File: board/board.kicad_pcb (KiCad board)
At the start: 2 copper layers, 21 x 13 mm, 1 part

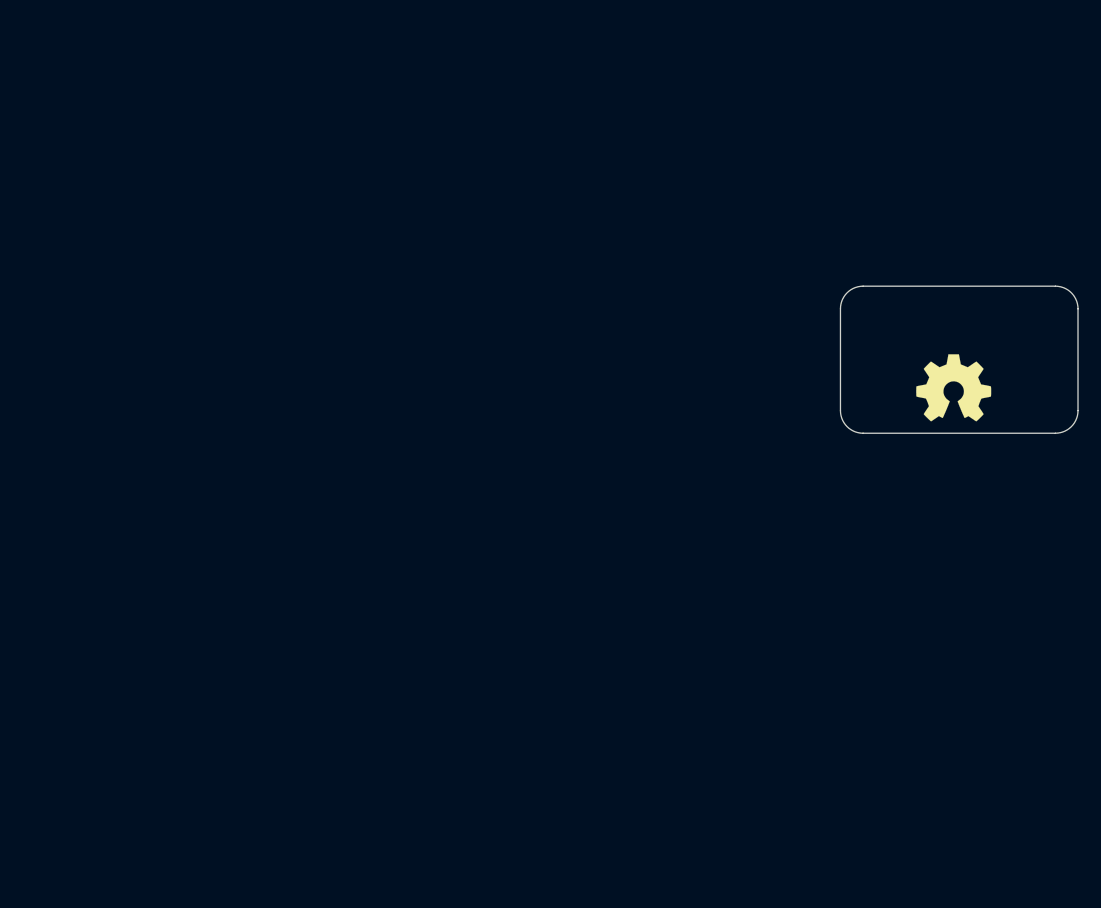
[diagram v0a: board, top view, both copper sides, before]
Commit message: added schematic and footprint from legacy project
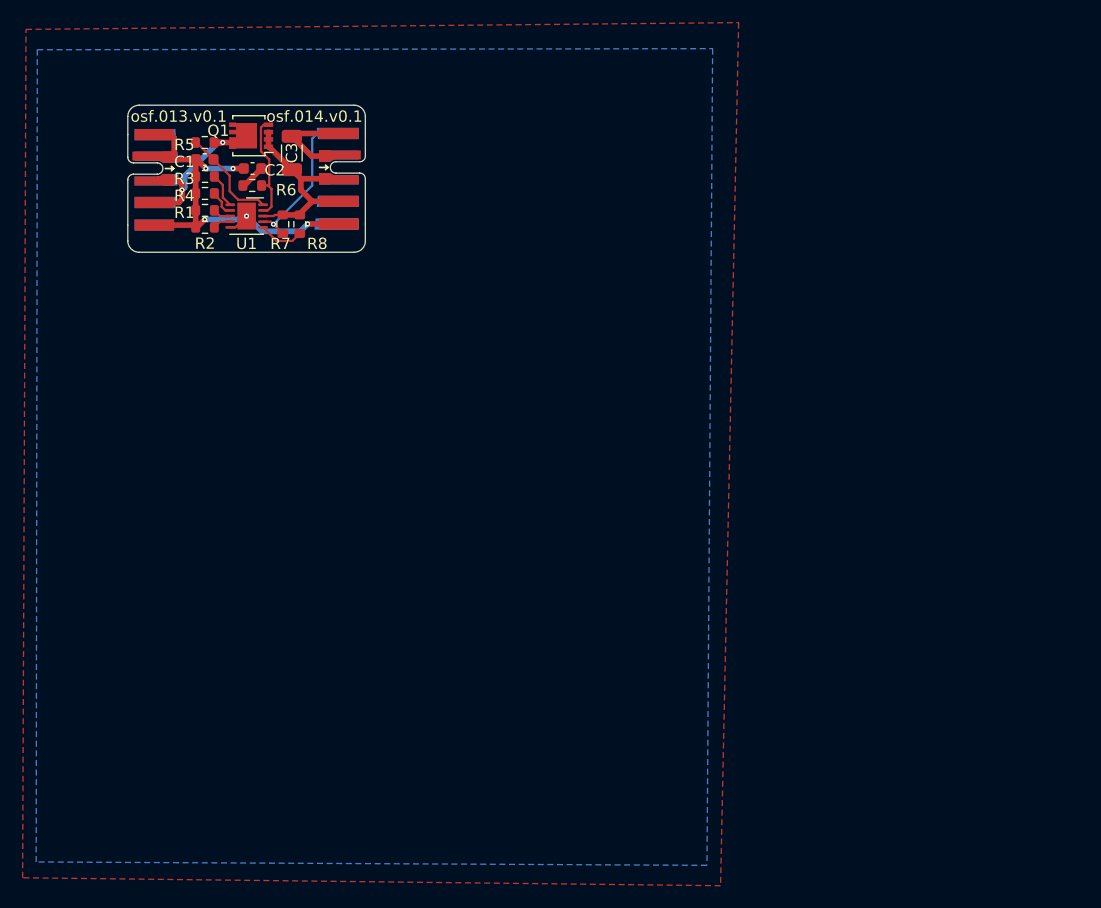
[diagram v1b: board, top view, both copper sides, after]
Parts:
- added C1: 47nF, Capacitor_SMD:C_0603_1608Metric, F.Cu at (83.8, 78.8)
- added C2: 47nF, Capacitor_SMD:C_0603_1608Metric, F.Cu at (88.0, 79.6)
- added C3: 1uF, Capacitor_SMD:C_1206_3216Metric, F.Cu at (91.5, 78.2)
- added J1: 013_PoE_rectified, on_edge:on_edge_2x05_device, F.Cu at (77.0, 80.6)
- added J2: 014_PoE_controlled, on_edge:on_edge_2x05_host, F.Cu at (98.0, 80.5)
- added Q1: PSMN5R2-60YL, Package_TO_SOT_SMD:LFPAK33, F.Cu at (87.9, 76.7)
- added R1: 49.9R, Resistor_SMD:R_0603_1608Metric, F.Cu at (83.8, 83.3)
- added R2: 118R, Resistor_SMD:R_0603_1608Metric, F.Cu at (83.8, 84.8)
- added R3: 0R, Resistor_SMD:R_0603_1608Metric, F.Cu at (83.8, 80.3)
- added R4: 0R, Resistor_SMD:R_0603_1608Metric, F.Cu at (83.8, 81.8)
- added R5: 8.2R, Resistor_SMD:R_0603_1608Metric, F.Cu at (83.8, 77.3)
- added R6: 3.3k, Resistor_SMD:R_0603_1608Metric, F.Cu at (88.0, 81.1)
- added R7: 100k, Resistor_SMD:R_0603_1608Metric, F.Cu at (90.7, 84.5)
- added R8: 100k, Resistor_SMD:R_0603_1608Metric, F.Cu at (92.2, 84.5)
- added U1: LT4275AIDDPBF-LT4275AIDDPBF, Package_DFN_QFN:DFN-10-1EP_3x3mm_P0.5mm_EP1.65x2.38mm, F.Cu at (87.5, 83.8)
- LOGO1: moved to B.Cu
- moved LOGO1 65.0 mm to (87.5, 81.0), turned to 180 degrees
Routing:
- net GND: track 0.00 -> 44.2 mm, vias 0 -> 5
- net /implementation/poe+_out: track 0.00 -> 17.1 mm
- net /implementation/poe+_in: track 0.00 -> 15.1 mm, vias 0 -> 2
- net /implementation/PG: track 0.00 -> 13.7 mm, vias 0 -> 1
- net Net-(Q1-Pad4): track 0.00 -> 9.70 mm
- net Net-(C1-Pad1): track 0.00 -> 9.06 mm
- net Net-(R8-Pad2): track 0.00 -> 4.02 mm
- net Net-(R3-Pad1): track 0.00 -> 3.08 mm
- net Net-(R4-Pad1): track 0.00 -> 2.33 mm
- net Net-(C2-Pad1): track 0.00 -> 2.25 mm
- net Net-(R2-Pad1): track 0.00 -> 1.61 mm
- net Net-(R1-Pad1): track 0.00 -> 1.61 mm
- added copper zone on B.Cu, net GND
- added copper zone on F.Cu, net GND
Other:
- outline, holes or cut-outs redrawn
- rule pad_to_mask_clearance: 0 -> 0.04
- board text added: "osf.013.v0.1"
- board text added: "osf.014.v0.1"
- board text added: "osf.b027.v0.1"
